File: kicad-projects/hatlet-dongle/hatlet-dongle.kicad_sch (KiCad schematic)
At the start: 9 parts, among them J1 Racklet_BackplaneSocket_02x06, J2 USB_C_Receptacle_USB2.0, J3 +12VDC, J4 +5VDC, J5 +5VSB, J6 GND

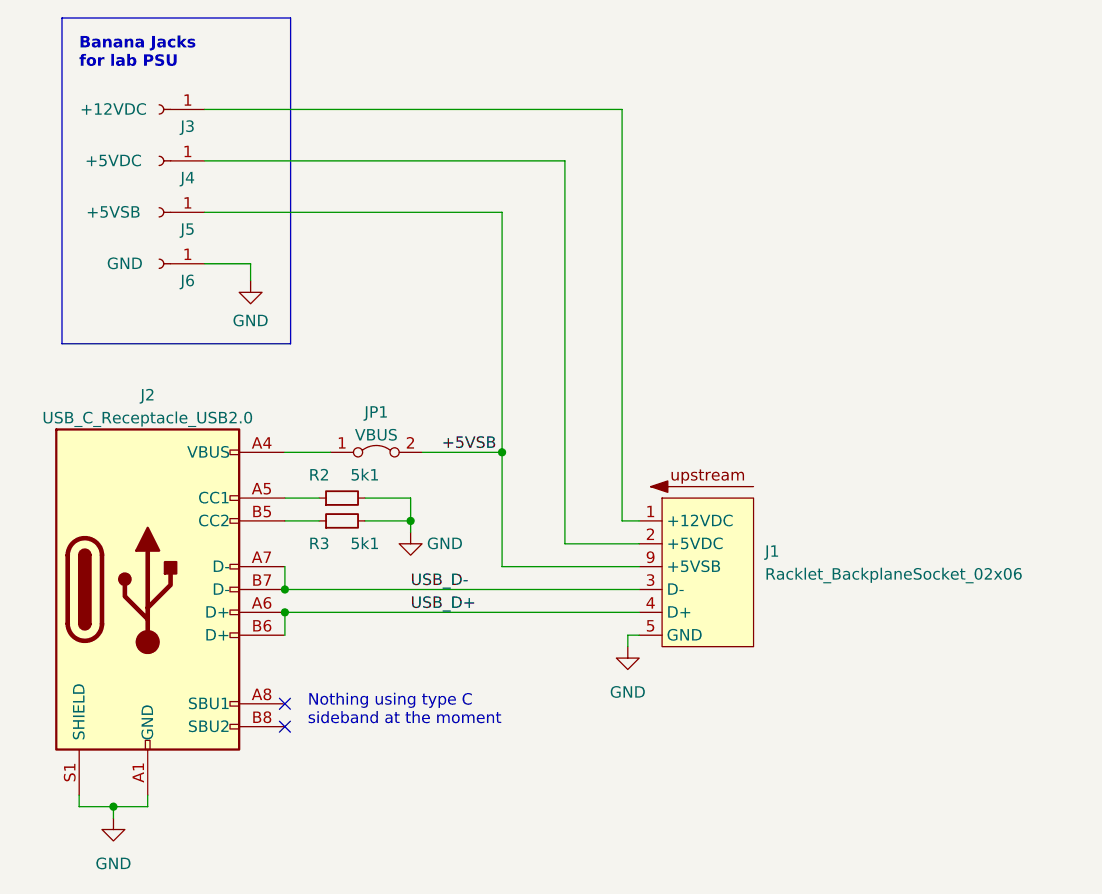
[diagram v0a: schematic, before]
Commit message: hatlet-dongle: use 3-position jumper to avoid PSU backpowering
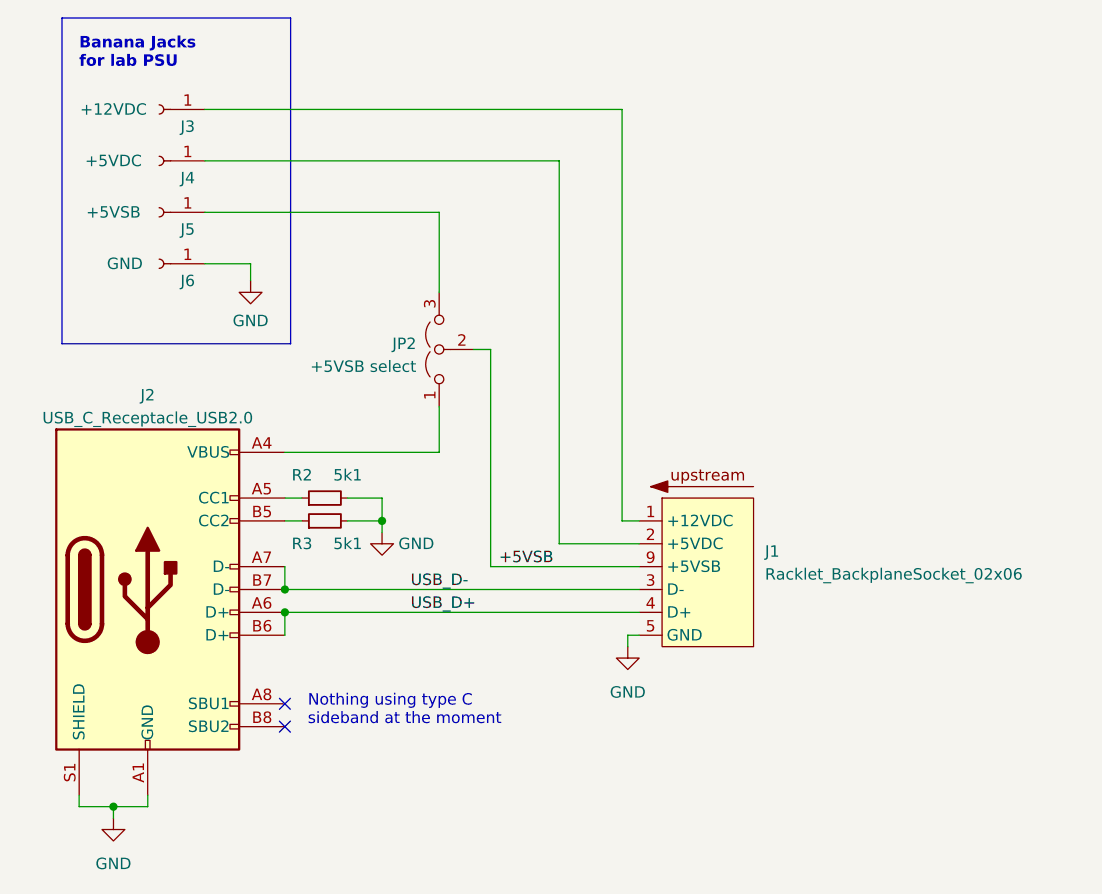
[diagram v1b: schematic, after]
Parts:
- removed JP1: VBUS, Connector_PinHeader_2.54mm:PinHeader_1x02_P2.54mm_Vertical, symbol Jumper:Jumper_2_Bridged
- added JP2: +5VSB select, Connector_PinHeader_2.54mm:PinHeader_1x03_P2.54mm_Vertical, symbol Jumper:Jumper_3_Open
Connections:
- net +5VSB: now also JP2.2 (C); no longer J5.1 (Pin_1)
- net at J2.A4 (VBUS), J2.A9 (VBUS), J2.B4 (VBUS)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: now also JP2.1 (A)
- new net: J5.1 (Pin_1), JP2.3 (B)
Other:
- title: Adapter - USB Socket to Type C Receptacle -> hatlet-dongle - Backplane Socket to Type C Receptacle
- moved on the sheet: R2, R3
